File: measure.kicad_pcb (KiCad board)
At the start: 2 copper layers, 10 parts, among them SW1 SW_Push_SPDT, SW2 SW_Push_SPDT, U1 ATtiny85-20S, U2 INA226, U3 L7805

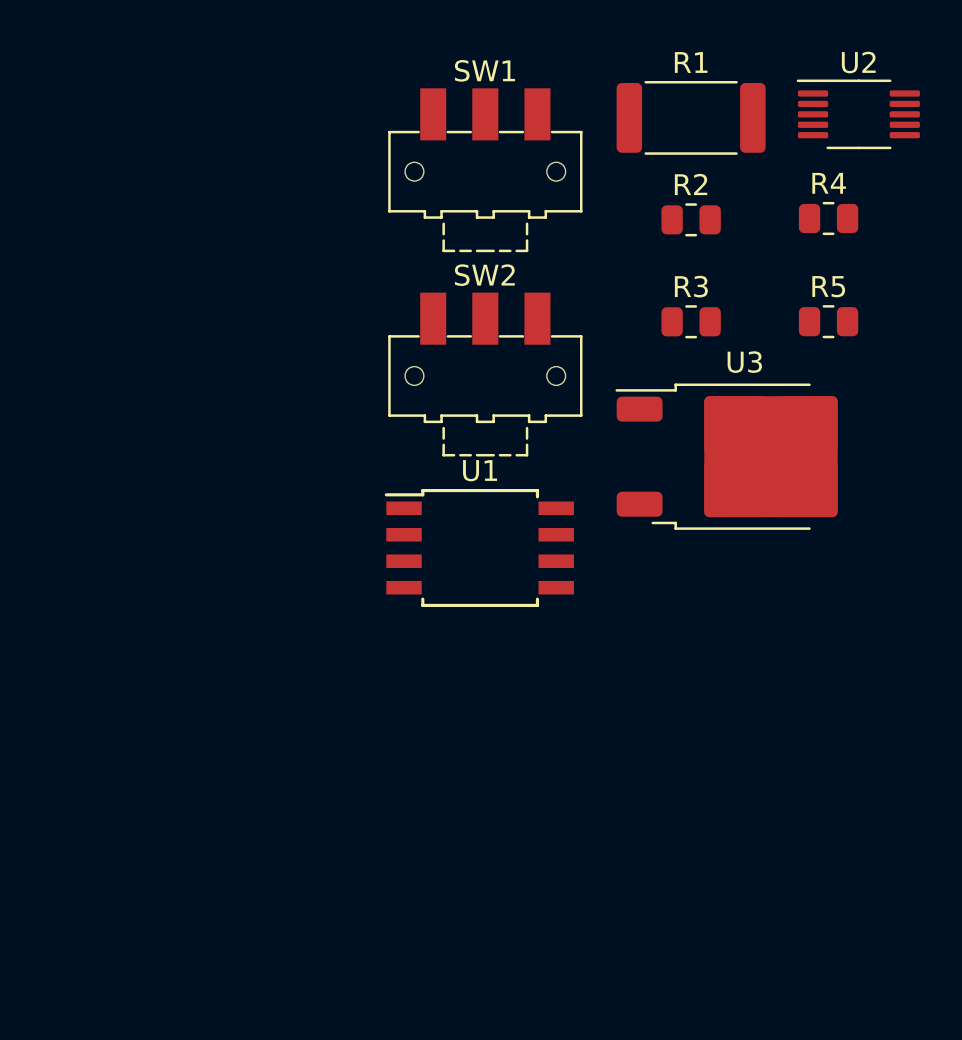
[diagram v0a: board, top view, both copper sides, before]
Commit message: component placement
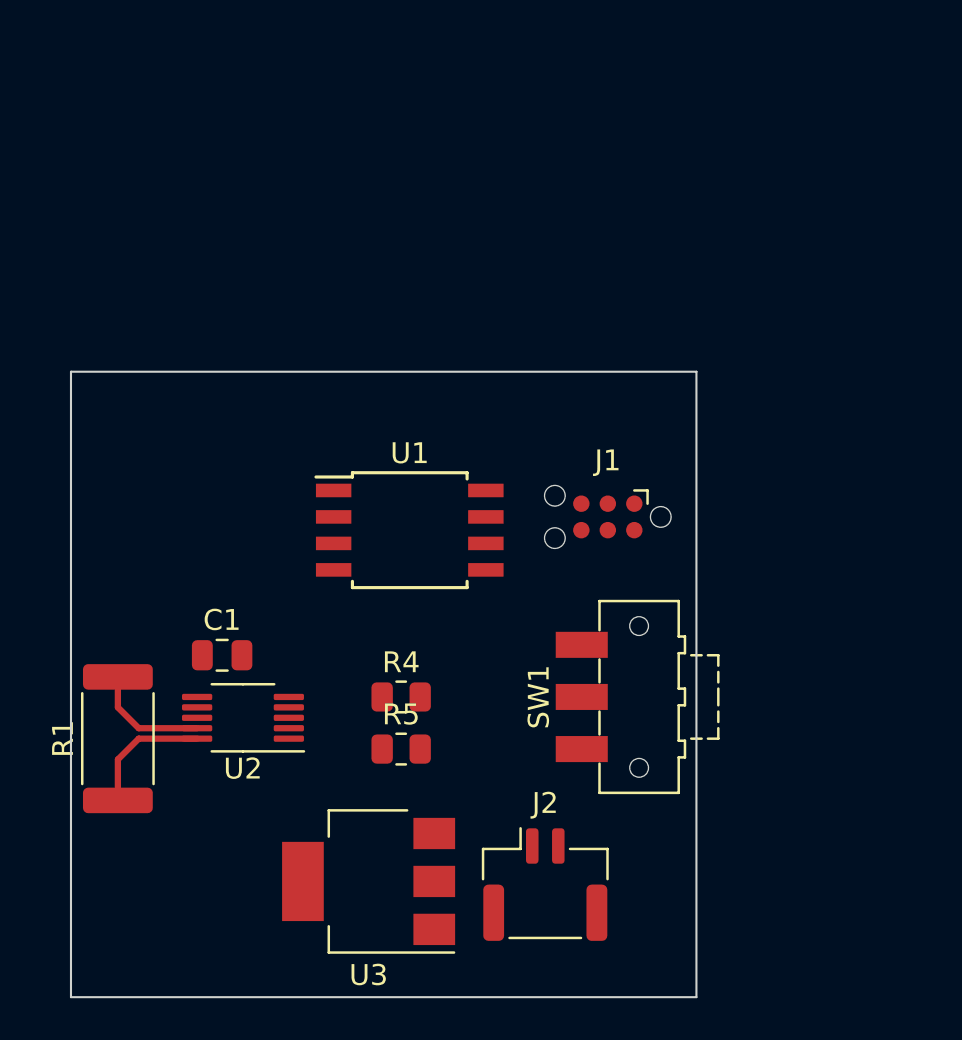
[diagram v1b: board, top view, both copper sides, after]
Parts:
- removed R2, R3: R, Resistor_SMD:R_0805_2012Metric
- removed SW2: SW_Push_SPDT, Button_Switch_SMD:SW_SPDT_CK-JS102011SAQN
- added C1: C, Capacitor_SMD:C_0805_2012Metric, F.Cu at (95.0, 87.0)
- added J1: Makeshift_SPI_header, Connector:Tag-Connect_TC2030-IDC-NL_2x03_P1.27mm_Vertical, F.Cu at (113.5, 80.4)
- added J2: Battery_conn, Connector_JST:JST_GH_SM02B-GHS-TB_1x02-1MP_P1.25mm_Horizontal, F.Cu at (110.5, 98.0)
- SW1: value SW_Push_SPDT -> SW_SPST
- U3: value L7805 -> AMS1117-3.3; footprint Package_TO_SOT_SMD:TO-252-2 -> Package_TO_SOT_SMD:SOT-223-3_TabPin2
- moved U2 41.4 mm to (96.0, 90.0), turned to 180 degrees
- moved R1 40.5 mm to (90.0, 91.0), turned to 90 degrees
- moved R4 30.8 mm to (103.6, 89.0)
- moved R5 29.0 mm to (103.6, 91.5)
- moved U3 27.2 mm to (102.0, 97.8), turned to 180 degrees
- moved SW1 26.3 mm to (115.0, 89.0), turned to 90 degrees
- moved U1 3.48 mm to (104.0, 81.0)
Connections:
- R1 pad 1: unconnected-(R1-Pad1) -> VS
- R1 pad 2: unconnected-(R1-Pad2) -> /Vin-
- R4 pad 1: unconnected-(R4-Pad1) -> /SCK/SCL
- R4 pad 2: unconnected-(R4-Pad2) -> +5V
- R5 pad 1: unconnected-(R5-Pad1) -> /MOSI/SDA
- R5 pad 2: unconnected-(R5-Pad2) -> +5V
- SW1 pad 1: unconnected-(SW1-A-Pad1) -> +5V
- SW1 pad 2: unconnected-(SW1-B-Pad2) -> Net-(SW1-B)
- SW1 pad 3: unconnected-(SW1-C-Pad3) -> GND
- U1 pad 1: unconnected-(U1-~{RESET}/PB5-Pad1) -> /~{RST}
- U1 pad 4: unconnected-(U1-GND-Pad4) -> GND
- U1 pad 5: unconnected-(U1-AREF/PB0-Pad5) -> /MOSI/SDA
- U1 pad 6: unconnected-(U1-PB1-Pad6) -> /MISO
- U1 pad 7: unconnected-(U1-PB2-Pad7) -> /SCK/SCL
- U1 pad 8: unconnected-(U1-VCC-Pad8) -> +5V
- U2 pad 1: unconnected-(U2-A1-Pad1) -> GND
- U2 pad 10: unconnected-(U2-Vin+-Pad10) -> VS
- U2 pad 2: unconnected-(U2-A0-Pad2) -> GND
- U2 pad 4: unconnected-(U2-SDA-Pad4) -> /MOSI/SDA
- U2 pad 5: unconnected-(U2-SCL-Pad5) -> /SCK/SCL
- U2 pad 6: unconnected-(U2-VS-Pad6) -> +5V
- U2 pad 7: unconnected-(U2-GND-Pad7) -> GND
- U2 pad 8: unconnected-(U2-Vbus-Pad8) -> VS
- U2 pad 9: unconnected-(U2-Vin--Pad9) -> /Vin-
- U3 pad 1: unconnected-(U3-IN-Pad1) -> GND
- U3 pad 2: unconnected-(U3-GND-Pad2) -> Net-(SW1-B)
- U3 pad 3: unconnected-(U3-OUT-Pad3) -> VCC
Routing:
- net VS: track 0.00 -> 6.18 mm
- net /Vin-: track 0.00 -> 5.68 mm
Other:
- board outline added: 30 x 30 mm

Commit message: Shunt looks good
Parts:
- added TP1: IN, TestPoint:TestPoint_Pad_4.0x4.0mm, F.Cu at (91.0, 96.0)
- added TP2: OUT, TestPoint:TestPoint_Pad_4.0x4.0mm, F.Cu at (91.0, 81.0)
- R4, R5: footprint Resistor_SMD:R_0805_2012Metric -> Resistor_SMD:R_0603_1608Metric
- moved R5 6.78 mm to (105.5, 85.0)
- moved R4 4.24 mm to (102.2, 85.0), turned to 180 degrees
- moved U2 3.01 mm to (98.0, 87.8)
- moved R1 2.69 mm to (91.0, 88.5)
- moved C1 2.47 mm to (96.5, 85.0)
- moved U1 2.00 mm to (102.0, 81.0)
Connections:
- net VS renamed /Vin+
- J1 pad 2: /MISO -> /MOSI/SDA
- J1 pad 4: /SCK/SCL -> /MISO
- J1 pad 6: /MOSI/SDA -> /SCK/SCL
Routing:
- net Net-(SW1-B): track 0.00 -> 22.8 mm
- net /~{RST}: track 0.00 -> 18.5 mm, vias 0 -> 2
- net /MOSI/SDA: track 0.00 -> 10.8 mm
- net /MISO: track 0.00 -> 9.12 mm
- net /SCK/SCL: track 0.00 -> 6.84 mm
- net VCC: track 0.00 -> 4.95 mm
- net /Vin+: track 6.18 -> 10.0 mm
- net GND: track 0.00 -> 1.74 mm, vias 0 -> 14
- net /Vin-: track 5.68 -> 6.93 mm
- added copper zone on F.Cu, net /Vin+
- added copper zone on F.Cu, net /Vin-
- added copper zone on B.Cu, net GND
- added copper zone on F.Cu, net GND

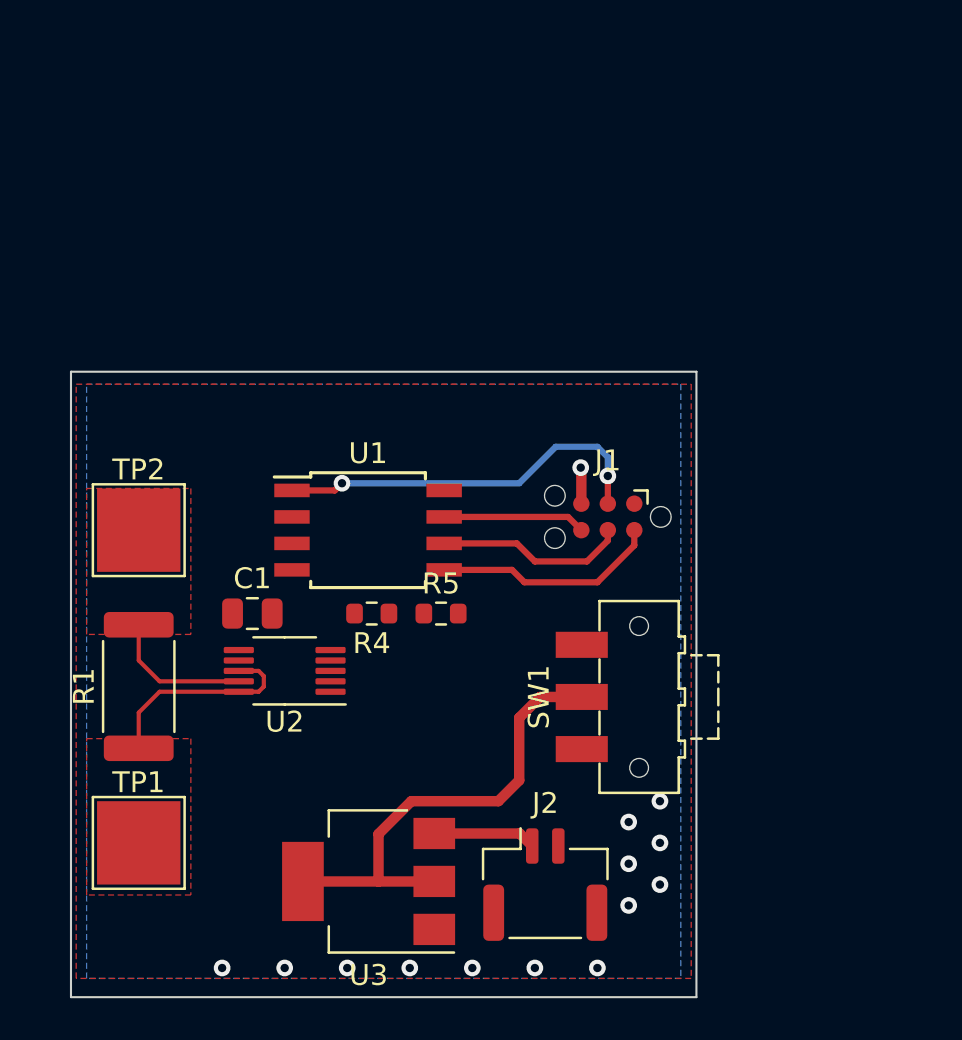
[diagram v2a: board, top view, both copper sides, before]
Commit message: I2C done, new place for tiny85
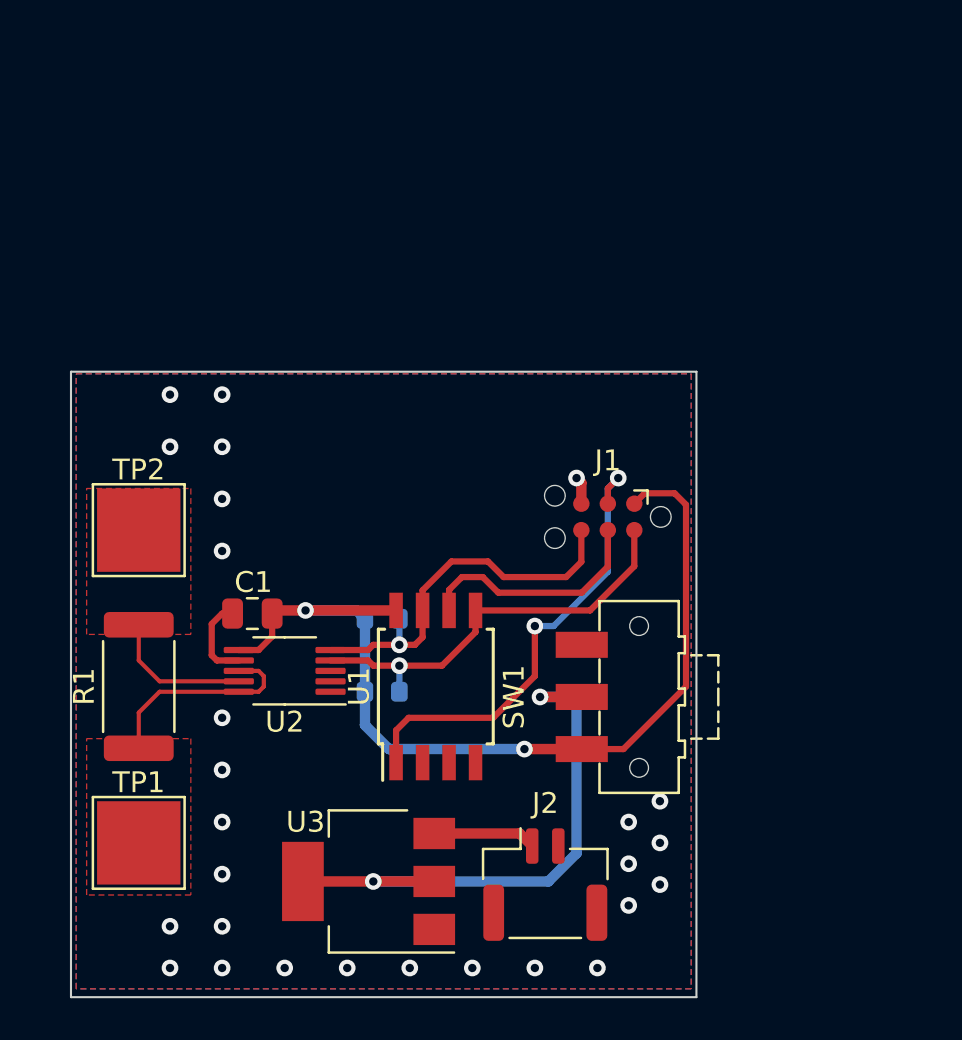
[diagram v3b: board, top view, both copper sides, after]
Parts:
- R4, R5: moved to B.Cu
- moved U1 8.17 mm to (105.2, 88.5), turned to 90 degrees
- moved R5 4.70 mm to (102.7, 88.8), turned to 180 degrees
- moved R4 0.56 mm to (102.7, 85.2)
- turned C1 to 180 degrees
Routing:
- net +5V: track 0.00 -> 45.8 mm, vias 0 -> 2
- net /SCK/SCL: track 6.84 -> 18.5 mm, vias 0 -> 1
- net /MOSI/SDA: track 10.8 -> 20.2 mm, vias 0 -> 1
- net Net-(SW1-B): track 22.8 -> 27.6 mm, vias 0 -> 2
- net GND: track 1.74 -> 5.86 mm, vias 14 -> 27
- net /~{RST}: track 18.5 -> 22.4 mm
- net /MISO: track 9.12 -> 11.4 mm
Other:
- board text added: "NAME"

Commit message: Lets name it tinyzinger
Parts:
- added G***: LOGO, sche:tinyZINGER, F.Cu at (102.0, 80.0)
- added G***: LOGO, sche:tinyZINGER, B.Cu at (106.8, 101.0)
- added U4: SSD1306_OLEDModule, sche:SSD1306_OLEDModule, B.Cu at (106.5, 75.5)
- moved R4 1.65 mm to (104.3, 85.2), turned to 0 degrees
- moved R5 1.65 mm to (104.3, 88.8), turned to 0 degrees
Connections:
- net +5V renamed +3V3
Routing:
- net +3V3: track 45.8 -> 73.4 mm
- net /MOSI/SDA: track 20.2 -> 36.5 mm
- net /SCK/SCL: track 18.5 -> 32.6 mm
- net /~{RST}: track 22.4 -> 23.7 mm
- net GND: track 5.86 -> 6.72 mm, vias 27 -> 1
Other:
- board text added: "BAT"
- board text added: "GND"
- board text added: "IN+"
- board text added: "IN-"
- board text added: "SCL"
- board text added: "SDA"
- board text added: "SPI"
- board text added: "VCC"
